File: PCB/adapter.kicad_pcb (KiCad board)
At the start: 2 copper layers, 41 x 31 mm, 8 parts

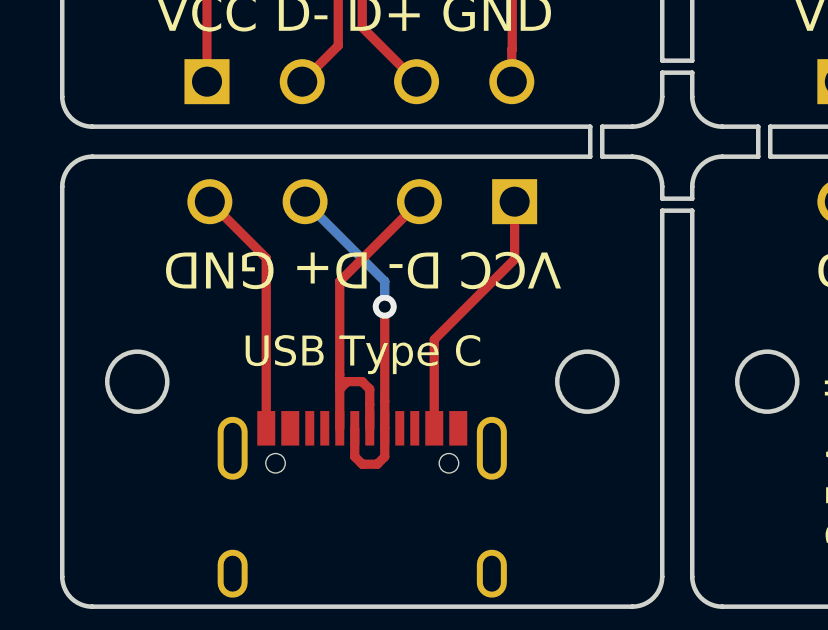
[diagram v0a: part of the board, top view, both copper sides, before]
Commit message: update type c
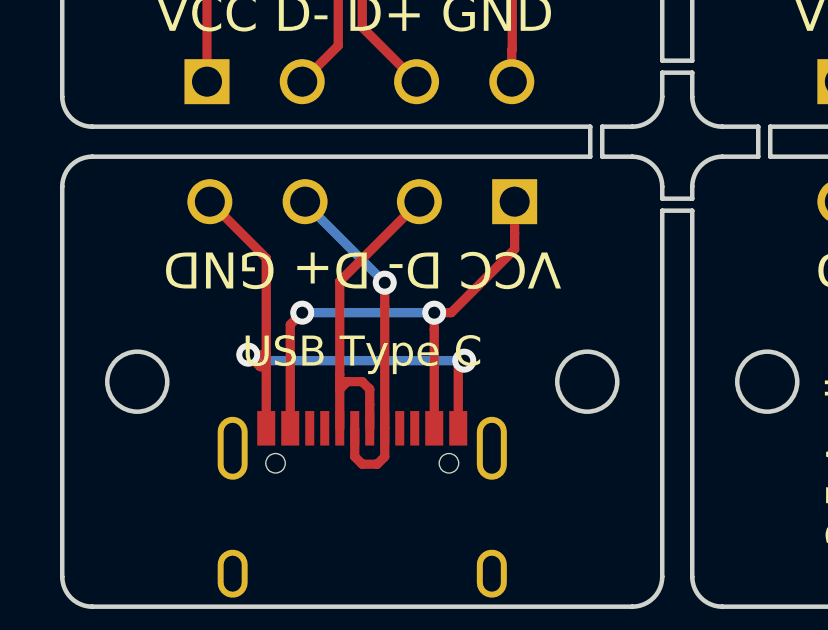
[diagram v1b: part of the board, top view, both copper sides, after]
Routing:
- net (no net): track 139.1 -> 158.8 mm, vias 1 -> 5
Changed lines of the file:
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@@
     (thickness 1.6)
     (drawings 60)
-    (tracks 59)
+    (tracks 79)
     (zones 0)
     (modules 8)
@@
   (segment (start 25 21) (end 25 26.69) (width 0.31) (layer F.Cu) (net 0))
   (segment (start 21.8 34.38) (end 19.92 32.5) (width 0.31) (layer F.Cu) (net 0))
-  (segment (start 21.8 40.055) (end 21.8 34.38) (width 0.31) (layer F.Cu) (net 0))
-  (segment (start 27.4 40.055) (end 27.4 37.1) (width 0.31) (layer F.Cu) (net 0))
-  (segment (start 30.08 34.42) (end 30.08 32.5) (width 0.31) (layer F.Cu) (net 0))
-  (segment (start 27.4 37.1) (end 30.08 34.42) (width 0.31) (layer F.Cu) (net 0))
   (segment (start 24.75 40.055) (end 24.75 41) (width 0.31) (layer F.Cu) (net 0))
   (segment (start 24.75 41) (end 25 41.25) (width 0.31) (layer F.Cu) (net 0))
@@
   (segment (start 24.5 38.5) (end 25 38.5) (width 0.31) (layer F.Cu) (net 0))
   (segment (start 24.25 38.5) (end 24.5 38.5) (width 0.31) (layer F.Cu) (net 0))
-  (segment (start 25.75 40.055) (end 25.75 39.17) (width 0.31) (layer F.Cu) (net 0))
-  (via (at 25.75 36) (size 0.8) (drill 0.4) (layers F.Cu B.Cu) (net 0))
-  (segment (start 25.75 39.17) (end 25.75 36) (width 0.31) (layer F.Cu) (net 0))
-  (segment (start 25.75 35.155) (end 23.095 32.5) (width 0.31) (layer B.Cu) (net 0))
-  (segment (start 25.75 36) (end 25.75 35.155) (width 0.31) (layer B.Cu) (net 0))
+  (via (at 25.75 35.2) (size 0.8) (drill 0.4) (layers F.Cu B.Cu) (net 0))
   (segment (start 51.08 33.56) (end 51.08 32.5) (width 0.31) (layer F.Cu) (net 0))
   (segment (start 51.08 36.53) (end 51.08 33.56) (width 0.31) (layer F.Cu) (net 0))
@@
   (segment (start 40.92 38.13) (end 42.59 39.8) (width 0.31) (layer F.Cu) (net 0))
   (segment (start 40.92 32.5) (end 40.92 38.13) (width 0.31) (layer F.Cu) (net 0))
+  (segment (start 25.75 36) (end 25.75 35.2) (width 0.31) (layer F.Cu) (net 0))
+  (segment (start 25.75 40.055) (end 25.75 36) (width 0.31) (layer F.Cu) (net 0))
+  (segment (start 23.095 32.545) (end 23.095 32.5) (width 0.31) (layer B.Cu) (net 0))
+  (segment (start 25.75 35.2) (end 23.095 32.545) (width 0.31) (layer B.Cu) (net 0))
+  (via (at 23 36.2) (size 0.8) (drill 0.4) (layers F.Cu B.Cu) (net 0))
+  (segment (start 22.6 40.055) (end 22.6 36.6) (width 0.31) (layer F.Cu) (net 0))
+  (segment (start 22.6 36.6) (end 23 36.2) (width 0.31) (layer F.Cu) (net 0))
+  (via (at 27.4 36.2) (size 0.8) (drill 0.4) (layers F.Cu B.Cu) (net 0))
+  (segment (start 23 36.2) (end 27.4 36.2) (width 0.31) (layer B.Cu) (net 0))
+  (segment (start 30.08 33.56) (end 30.08 32.5) (width 0.31) (layer F.Cu) (net 0))
+  (segment (start 30.08 34.085685) (end 30.08 33.56) (width 0.31) (layer F.Cu) (net 0))
+  (segment (start 27.965685 36.2) (end 30.08 34.085685) (width 0.31) (layer F.Cu) (net 0))
+  (segment (start 27.4 36.2) (end 27.965685 36.2) (width 0.31) (layer F.Cu) (net 0))
+  (segment (start 27.4 36.765685) (end 27.4 40.055) (width 0.31) (layer F.Cu) (net 0))
+  (segment (start 27.4 36.2) (end 27.4 36.765685) (width 0.31) (layer F.Cu) (net 0))
+  (via (at 28.4 37.8) (size 0.8) (drill 0.4) (layers F.Cu B.Cu) (net 0))
+  (segment (start 28.2 40.055) (end 28.2 38) (width 0.31) (layer F.Cu) (net 0))
+  (segment (start 28.2 38) (end 28.4 37.8) (width 0.31) (layer F.Cu) (net 0))
+  (via (at 21.2 37.6) (size 0.8) (drill 0.4) (layers F.Cu B.Cu) (net 0))
+  (segment (start 28.4 37.8) (end 21.4 37.8) (width 0.31) (layer B.Cu) (net 0))
+  (segment (start 21.4 37.8) (end 21.2 37.6) (width 0.31) (layer B.Cu) (net 0))
+  (segment (start 21.765685 37.6) (end 21.8 37.6) (width 0.31) (layer F.Cu) (net 0))
+  (segment (start 21.2 37.6) (end 21.765685 37.6) (width 0.31) (layer F.Cu) (net 0))
+  (segment (start 21.8 37.6) (end 21.8 34.38) (width 0.31) (layer F.Cu) (net 0))
+  (segment (start 21.6 38) (end 21.8 38) (width 0.31) (layer F.Cu) (net 0))
+  (segment (start 21.2 37.6) (end 21.6 38) (width 0.31) (layer F.Cu) (net 0))
+  (segment (start 21.8 40.055) (end 21.8 38) (width 0.31) (layer F.Cu) (net 0))
+  (segment (start 21.8 38) (end 21.8 37.6) (width 0.31) (layer F.Cu) (net 0))
 )

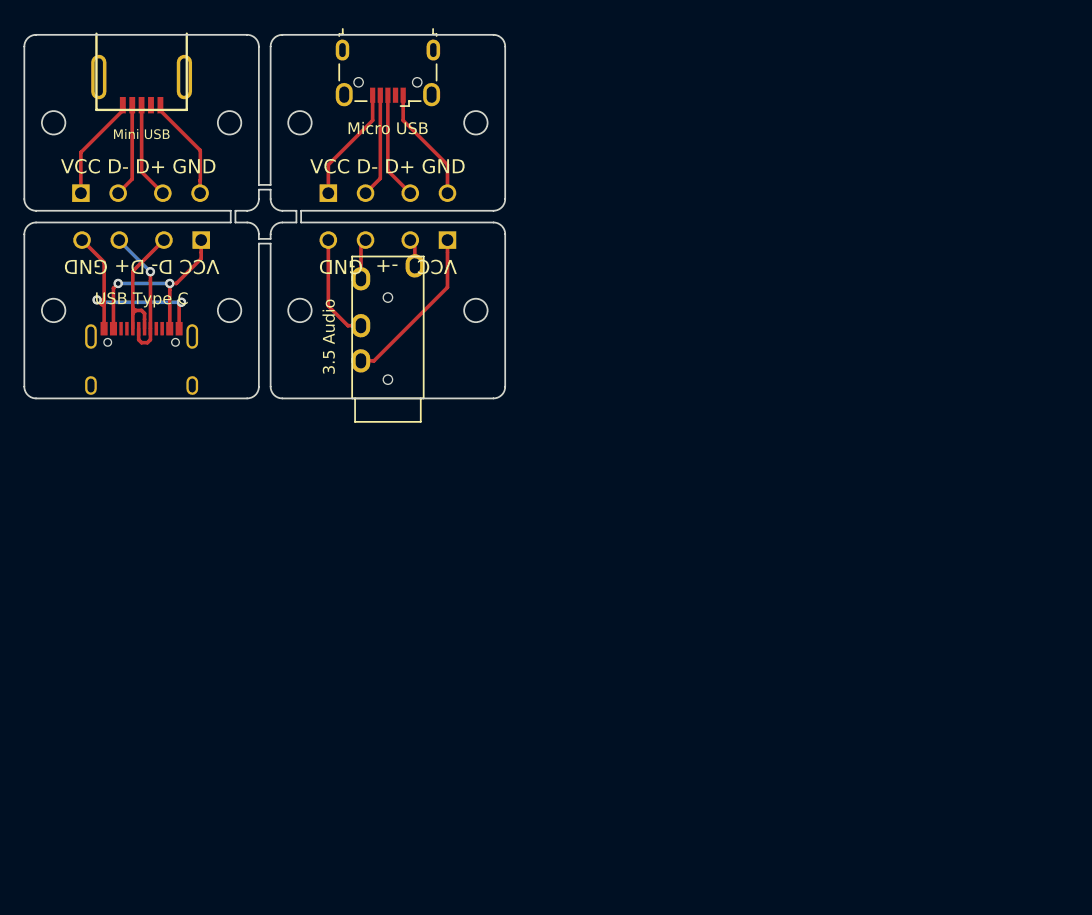
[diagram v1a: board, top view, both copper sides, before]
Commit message: fix wrong pins
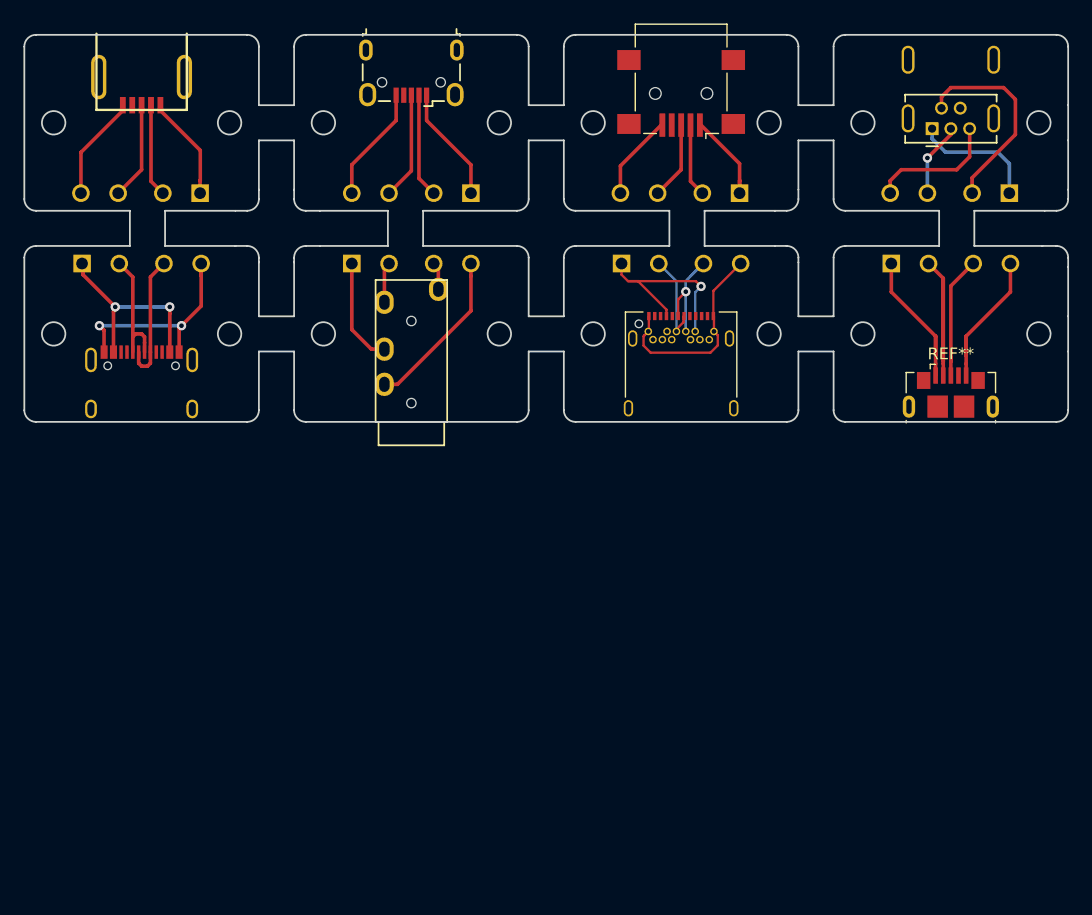
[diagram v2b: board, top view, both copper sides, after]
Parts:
- removed the ? at (46.0, 28.5)
- added  : , Connector_USB:USB_C_Receptacle_Amphenol_12401548E4-2A, F.Cu at (71.0, 44.0)
- added  : , Connector_USB:USB_Mini-B_Tensility_54-00023_Vertical, F.Cu at (92.4, 18.0)
- added  : , Connector_USB:USB_Mini-B_Tensility_54-00023_Vertical, F.Cu at (92.4, 23.0)
- added  : , Connector_USB:USB_Mini-B_Lumberg_2486_01_Horizontal, F.Cu at (71.0, 20.0)
- added ?: , Wire_Pads:SolderWirePad_4xInline_0-8mmDrill, F.Cu at (94.0, 34.5)
- added ?: , , F.Cu at (1.20, -0.50)
- added ?: , , F.Cu at (69.0, 1.00)
- added ?: , , F.Cu at (46.0, 1.00)
- added ?: , Wire_Pads:SolderWirePad_4xInline_0-8mmDrill, F.Cu at (71.0, 34.5)
- added ?: , Wire_Pads:SolderWirePad_4xInline_0-8mmDrill, F.Cu at (93.9, 28.5)
- added ?: , Wire_Pads:SolderWirePad_4xInline_0-8mmDrill, F.Cu at (70.9, 28.5)
- added ?: , Wire_Pads:SolderWirePad_4xInline_0-8mmDrill, F.Cu at (48.0, 28.5)
- added REF**: USB_Micro-B_GCT_USB3076-30-A, Connector_USB:USB_Micro-B_GCT_USB3076-30-A, F.Cu at (94.0, 45.5)
- moved ? 2.83 mm to (48.0, 48.0)
- moved ? 2.83 mm to (48.0, 34.5), turned to 0 degrees
- moved ? 2.00 mm to (25.0, 34.5), turned to 0 degrees
- moved ? 2.00 mm to (25.0, 49.5)
- moved Micro USB 2.00 mm to (48.0, 18.2)
- turned ? to 180 degrees
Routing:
- net (no net): track 158.8 -> 343.6 mm, vias 5 -> 7
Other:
- board size 41 x 31 mm -> 89 x 33 mm
- net class Small added: clearance 0.2, trace_width 0.21, via_dia 0.4, via_drill 0.3

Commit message: add fpc version
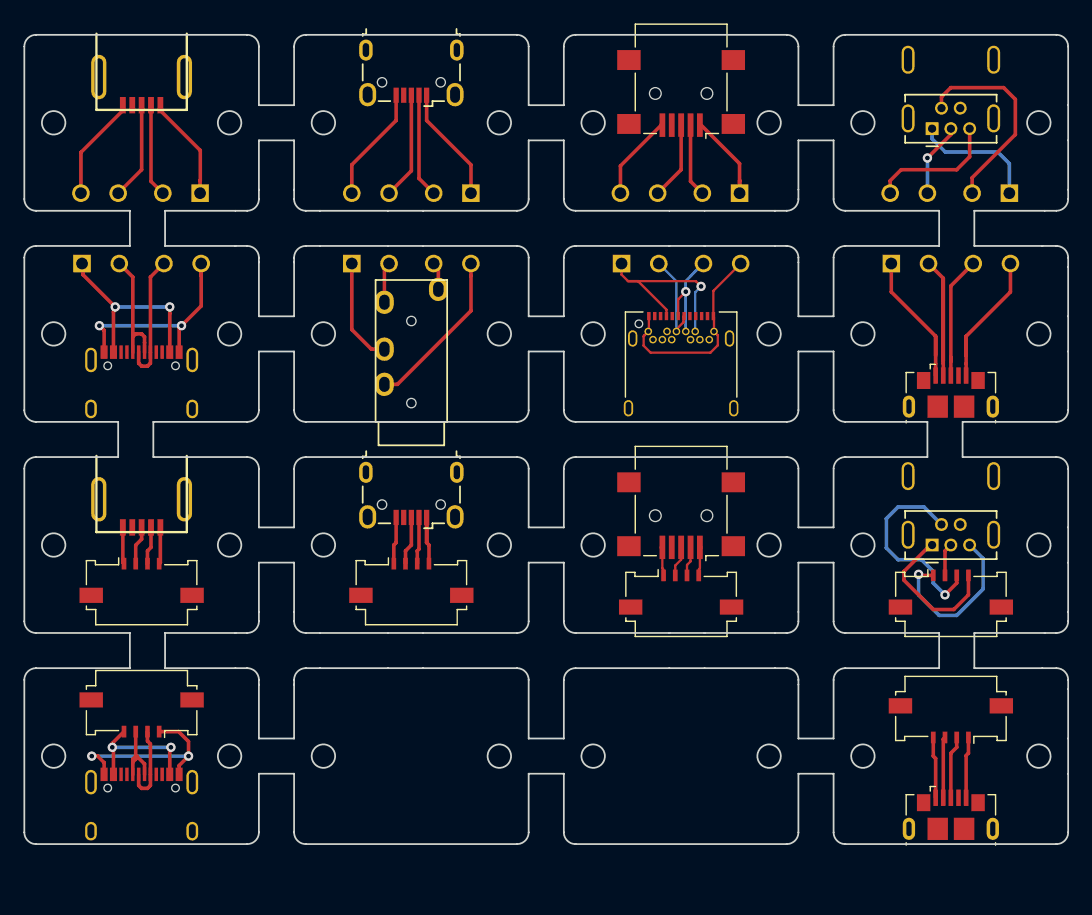
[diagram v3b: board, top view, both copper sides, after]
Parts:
- added  : , Connector_FFC-FPC:Molex_200528-0040_1x04-1MP_P1.00mm_Horizontal, F.Cu at (94.0, 74.0)
- added  : , Connector_USB:USB_Mini-B_Tensility_54-00023_Vertical, F.Cu at (92.4, 58.5)
- added  : , Connector_FFC-FPC:Molex_200528-0040_1x04-1MP_P1.00mm_Horizontal, F.Cu at (25.0, 73.5)
- added  : , Connector_FFC-FPC:Molex_200528-0040_1x04-1MP_P1.00mm_Horizontal, F.Cu at (94.0, 62.0)
- added  : , Connector_FFC-FPC:Molex_200528-0040_1x04-1MP_P1.00mm_Horizontal, F.Cu at (71.0, 62.0)
- added  : , Connector_FFC-FPC:Molex_200528-0040_1x04-1MP_P1.00mm_Horizontal, F.Cu at (48.0, 61.0)
- added  : , Connector_FFC-FPC:Molex_200528-0040_1x04-1MP_P1.00mm_Horizontal, F.Cu at (25.0, 61.0)
- added  : , Connector_USB:USB_Mini-B_Tensility_54-00023_Vertical, F.Cu at (92.4, 53.5)
- added  : , Connector_USB:USB_Micro-B_GCT_USB3076-30-A, F.Cu at (94.0, 81.5)
- added  : , Connector_USB:USB_Mini-B_Lumberg_2486_01_Horizontal, F.Cu at (71.0, 56.0)
- added ?: USB Type C, conn_usb:USB_TypeC_U31F-24SNA0201, F.Cu at (25.0, 85.5)
- added ?: , , F.Cu at (98.0, -9.00)
- added Micro USB: , Connectors_USB:USB_Micro-B_Wuerth-629105150521, F.Cu at (48.0, 54.2)
- added Mini USB: , keyboard_parts:USB_miniB_hirose_5S8, F.Cu at (25.0, 57.0)
-  : renamed from REF**; value USB_Micro-B_GCT_USB3076-30-A -> (none)
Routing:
- net (no net): track 343.6 -> 492.6 mm, vias 7 -> 13
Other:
- board size 89 x 33 mm -> 89 x 69 mm

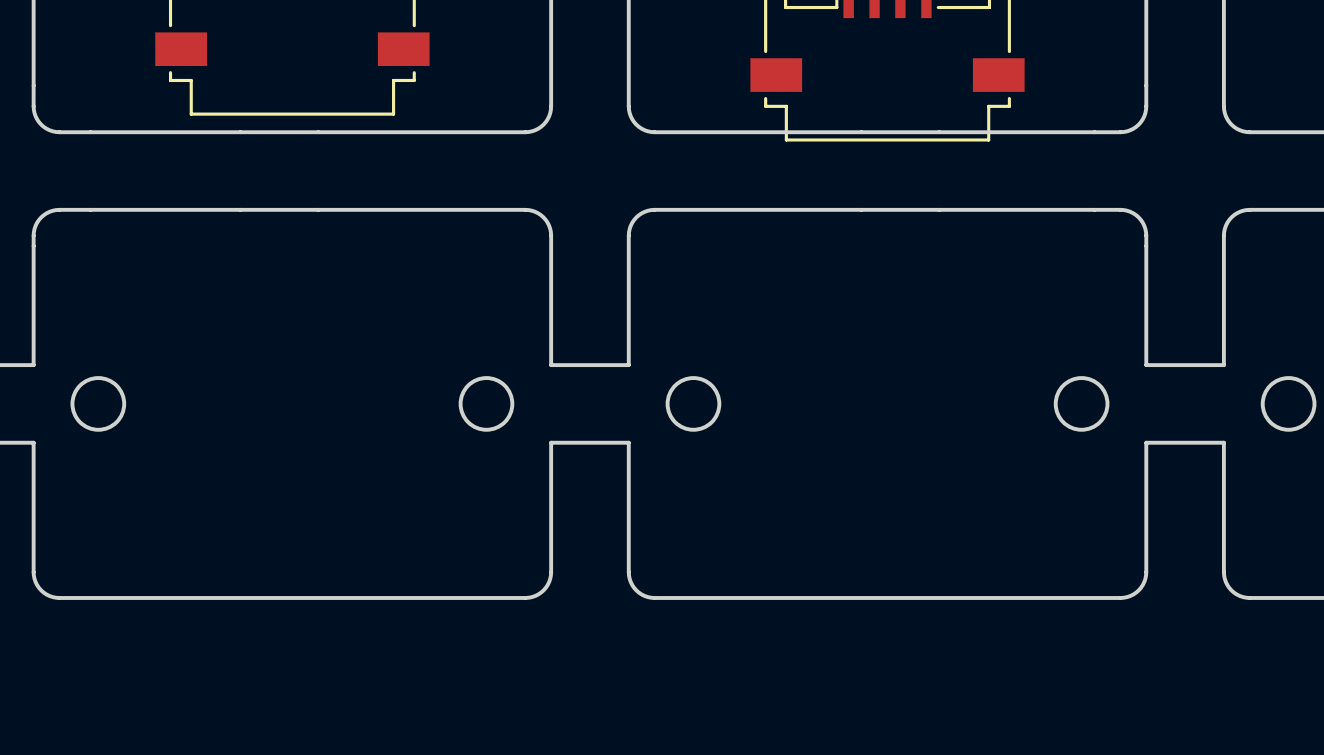
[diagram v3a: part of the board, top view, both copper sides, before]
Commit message: add fpc version
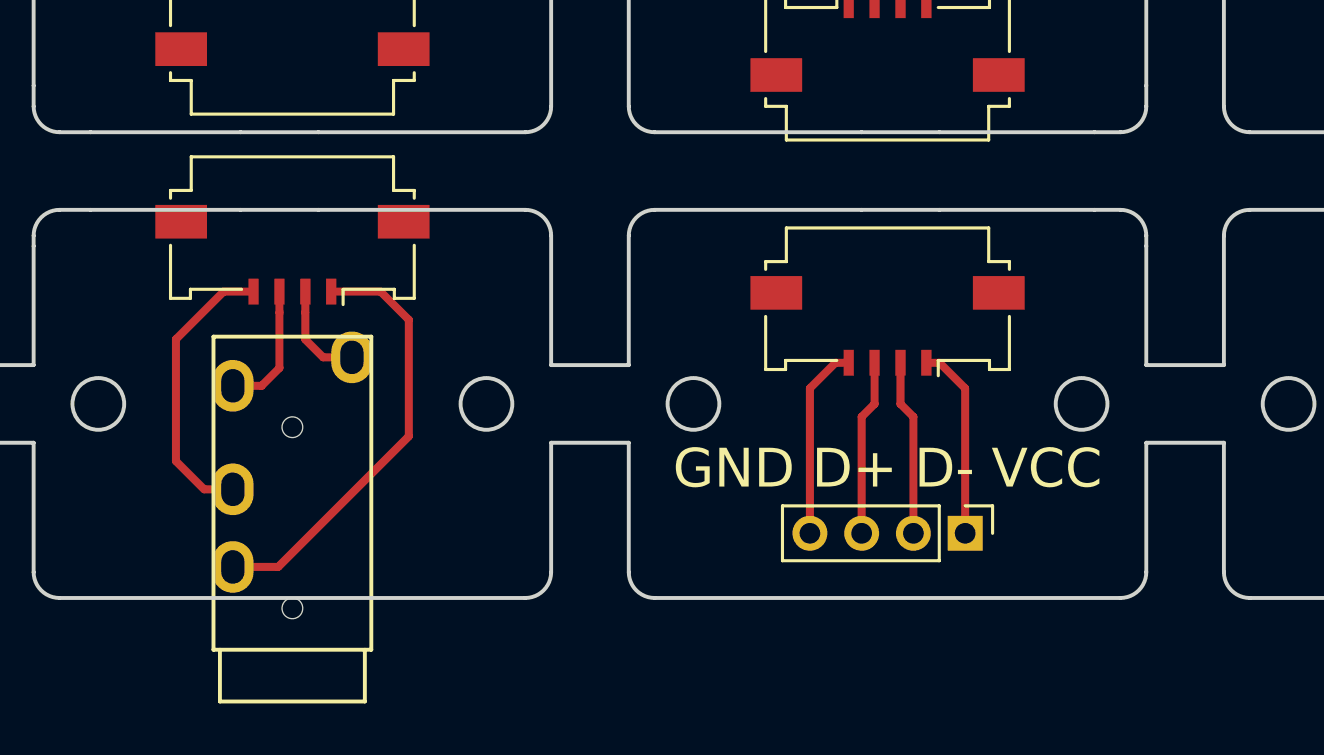
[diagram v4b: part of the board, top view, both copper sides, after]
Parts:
- added  : , Connector_PinHeader_2.00mm:PinHeader_1x04_P2.00mm_Vertical, F.Cu at (74.0, 81.5)
- added  : , Connector_FFC-FPC:Molex_200528-0040_1x04-1MP_P1.00mm_Horizontal, F.Cu at (71.0, 74.0)
- added  : , Connector_FFC-FPC:Molex_200528-0040_1x04-1MP_P1.00mm_Horizontal, F.Cu at (48.0, 71.2)
- added ?: , , F.Cu at (23.5, -6.50)
- added ?: 3.5 Audio, Keebio-Parts:TRRS-PJ-320A-no-Fmask, F.Cu at (48.0, 86.0)
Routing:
- net (no net): track 492.6 -> 558.2 mm
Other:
- board text added: "GND D+ D- VCC"
